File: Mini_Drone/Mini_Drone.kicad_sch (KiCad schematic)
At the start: 1 part, among them U5 STM32F722RETx

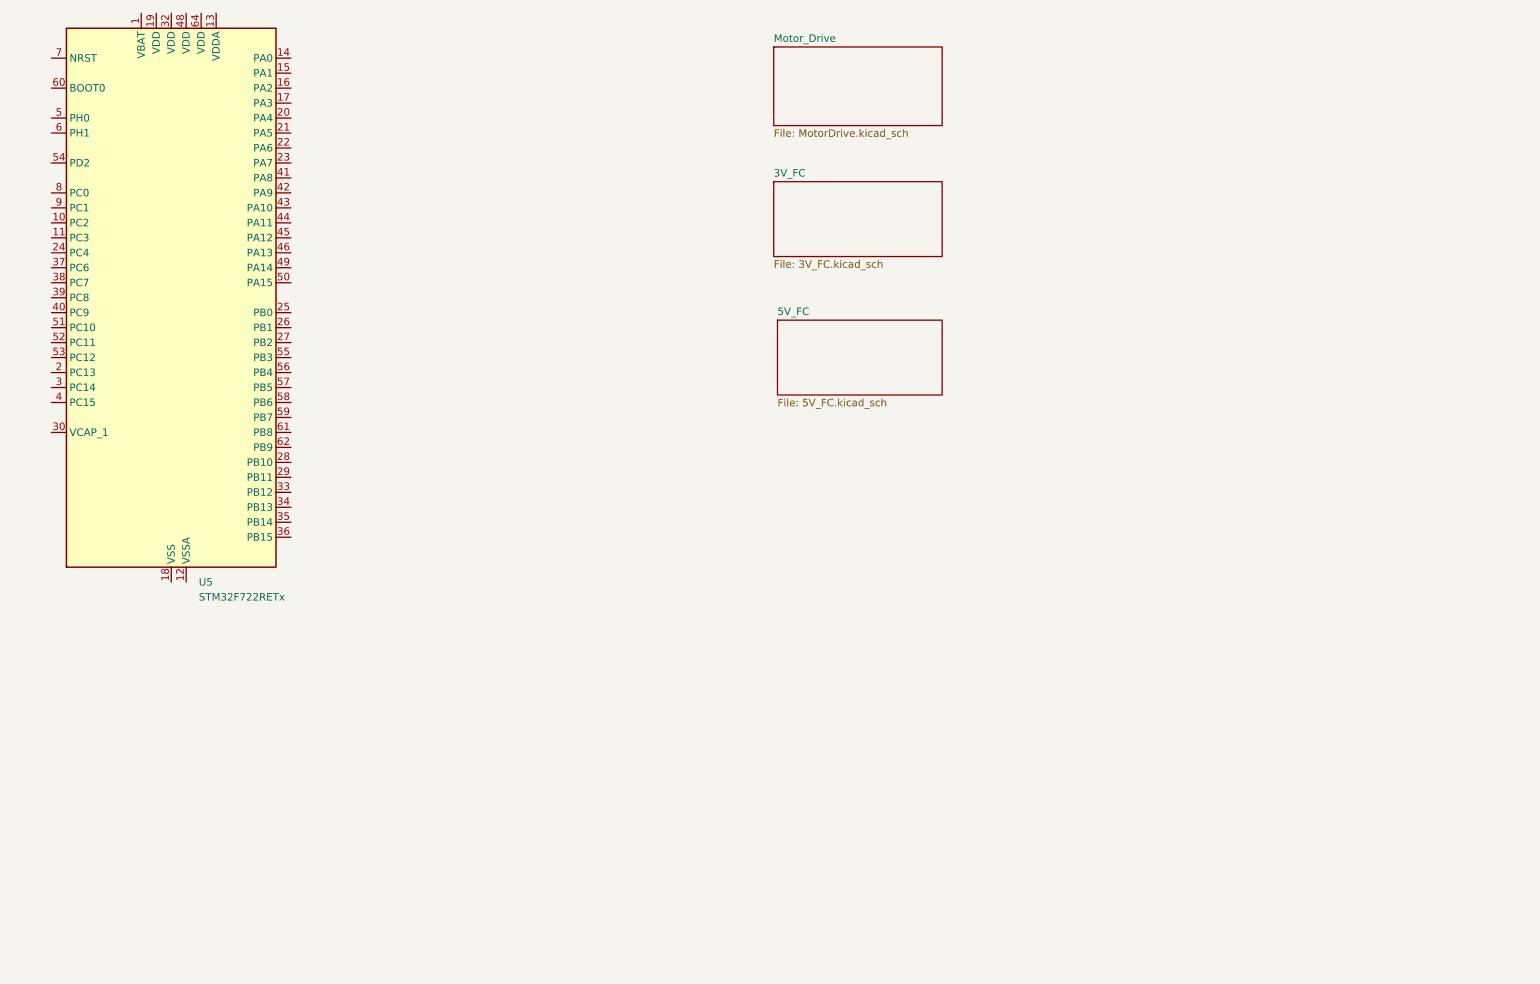
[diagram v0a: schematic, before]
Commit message: esp mini drone schematic
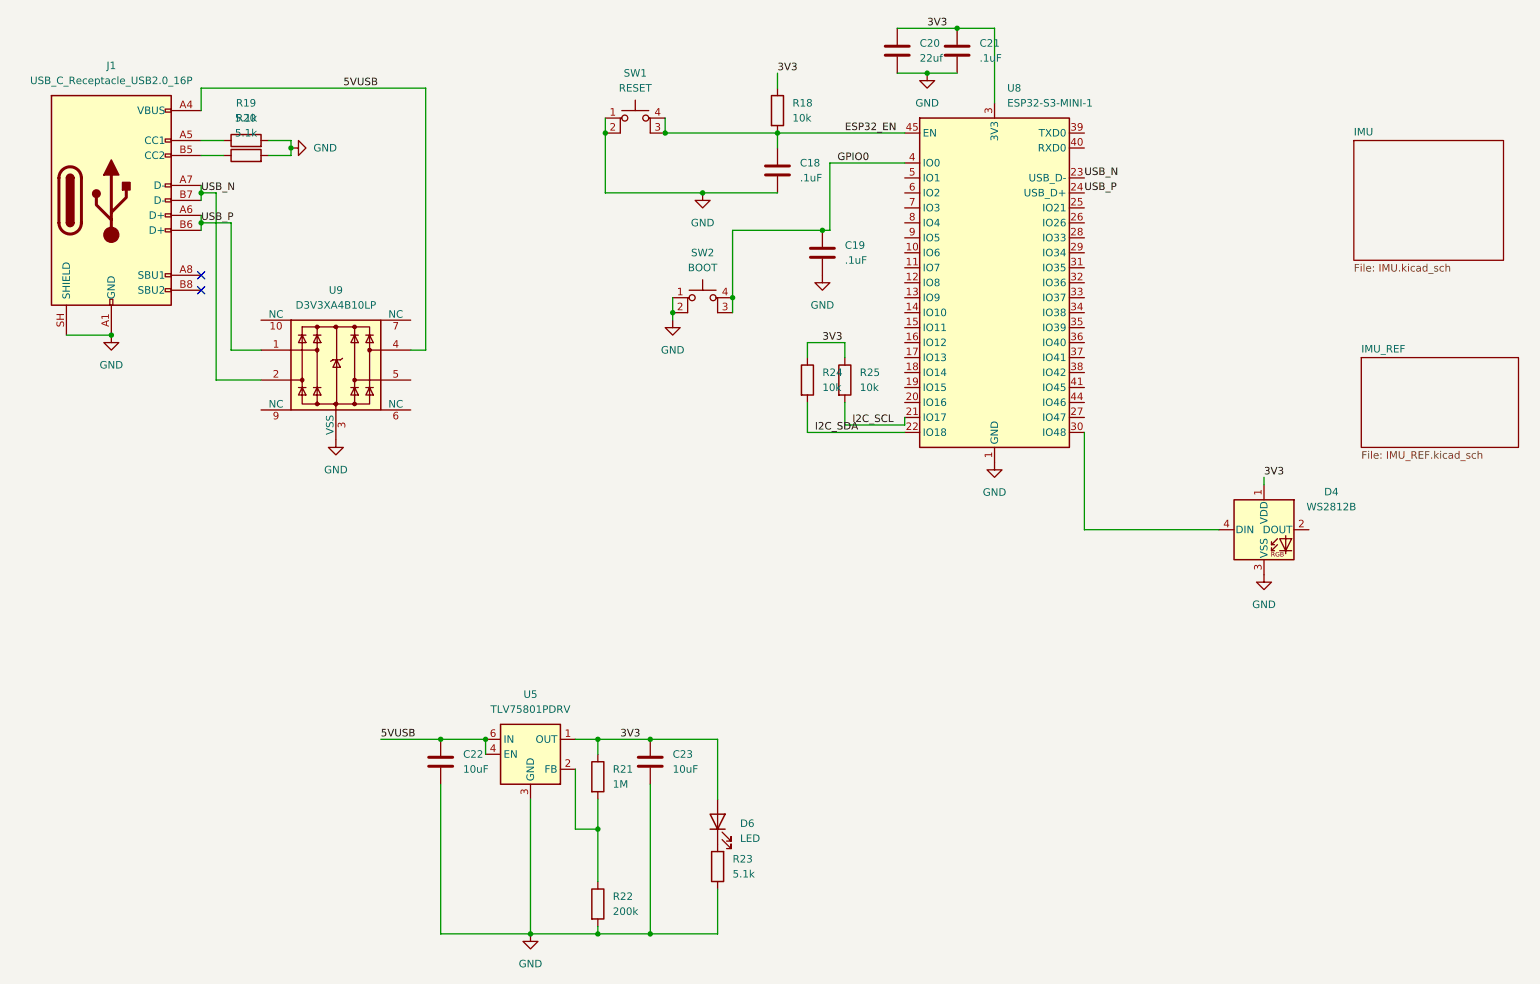
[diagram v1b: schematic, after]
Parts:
- removed U5: STM32F722RETx, Package_QFP:LQFP-64_10x10mm_P0.5mm, symbol MCU_ST_STM32F7:STM32F722RETx
- added C18, C19, C21: .1uF, Capacitor_SMD:C_0603_1608Metric_Pad1.08x0.95mm_HandSolder, symbol Device:C
- added C20: 22uf, Capacitor_SMD:C_0603_1608Metric_Pad1.08x0.95mm_HandSolder, symbol Device:C
- added C22, C23: 10uF, symbol Device:C
- added D4: WS2812B, LED_SMD:LED_WS2812B_PLCC4_5.0x5.0mm_P3.2mm, symbol LED:WS2812B
- added D6: LED, LED_SMD:LED_0603_1608Metric_Pad1.05x0.95mm_HandSolder, symbol Device:LED
- added J1: USB_C_Receptacle_USB2.0_16P, Connector_USB:USB_C_Receptacle_GCT_USB4105-xx-A_16P_TopMnt_Horizontal, symbol Connector:USB_C_Receptacle_USB2.0_16P
- added R18, R24, R25: 10k, Resistor_SMD:R_0603_1608Metric_Pad0.98x0.95mm_HandSolder, symbol Device:R
- added R19, R20, R23: 5.1k, symbol Device:R
- added R21: 1M, Resistor_SMD:R_0603_1608Metric_Pad0.98x0.95mm_HandSolder, symbol Device:R
- added R22: 200k, Resistor_SMD:R_0603_1608Metric_Pad0.98x0.95mm_HandSolder, symbol Device:R
- added SW1: RESET, Button_Switch_SMD:SW_SPST_PTS810, symbol Switch:SW_MEC_5E
- added SW2: BOOT, Button_Switch_SMD:SW_SPST_PTS810, symbol Switch:SW_MEC_5E
- added U5: TLV75801PDRV, Package_SON:WSON-6-1EP_2x2mm_P0.65mm_EP1x1.6mm, symbol Regulator_Linear:TLV75801PDRV
- added U8: ESP32-S3-MINI-1, RF_Module:ESP32-S2-MINI-1, symbol RF_Module:ESP32-S3-MINI-1
- added U9: D3V3XA4B10LP, Package_DFN_QFN:Diodes_UDFN-10_1x2.5mm_P0.5mm, symbol Power_Protection:D3V3XA4B10LP
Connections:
- new net: D6.1 (K), R23.2
- new net: R21.2, R22.1, U5.2 (FB)
- new net: J1.A5 (CC1), R19.1
- new net: J1.B5 (CC2), R20.1
- new net: D4.4 (DIN), U8.30 (IO48)
- new net 3V3: C20.1, C21.1, C23.1, D4.1 (VDD), D6.2 (A), R18.1, R21.1, R24.1, R25.1, U5.1 (OUT), U8.3 (3V3)
- new net 5VUSB: C22.1, J1.A4 (VBUS), J1.A9 (VBUS), J1.B4 (VBUS), J1.B9 (VBUS), U5.4 (EN), U5.6 (IN), U9.4
- new net ESP32_EN: C18.2, R18.2, SW1.3 (K), SW1.4 (A), U8.45 (EN)
- new net GND: C18.1, C19.2, C20.2, C21.2, C22.2, C23.2, D4.3 (VSS), J1.A1 (GND), J1.A12 (GND), J1.B1 (GND), J1.B12 (GND), J1.SH (SHIELD), R19.2, R20.2, R22.2, R23.1, SW1.1, SW1.2, SW2.1, SW2.2, U5.3 (GND), U5.7 (GND), U8.1 (GND), U8.2 (GND), U8.42 (GND), U8.43 (GND), U8.46 (GND), U8.47 (GND), U8.48 (GND), U8.49 (GND), U8.50 (GND), U8.51 (GND), U8.52 (GND), U8.53 (GND), U8.54 (GND), U8.55 (GND), U8.56 (GND), U8.57 (GND), U8.58 (GND), U8.59 (GND), U8.60 (GND), U8.61 (GND), U8.62 (GND), U8.63 (GND), U8.64 (GND), U8.65 (GND), U9.3 (VSS), U9.8 (VSS)
- new net GPIO0: C19.1, SW2.3 (K), SW2.4 (A), U8.4 (IO0)
- new net I2C_SCL: R25.2, U8.21 (IO17)
- new net I2C_SDA: R24.2, U8.22 (IO18)
- new net USB_N: J1.A7 (D-), J1.B7 (D-), U8.23 (USB_D-), U9.2
- new net USB_P: J1.A6 (D+), J1.B6 (D+), U8.24 (USB_D+), U9.1
- no-connect marks 0 -> 2
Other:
- removed sheet 3V_FC
- removed sheet 5V_FC
- removed sheet Motor_Drive
- added sheet IMU (IMU.kicad_sch)
- added sheet IMU_REF (IMU_REF.kicad_sch)
